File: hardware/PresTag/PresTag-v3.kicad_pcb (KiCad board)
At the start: 2 copper layers, 17 x 9 mm, 20 parts, among them J201 CONN_02X04, J301 Conn_01x01, J302 Conn_01x01, J303 Conn_01x01, J304 Conn_01x01, J401 CONN_01X02, Q501 Q_NPN_BEC, U1 at25ex321D-UUN, U2 LPS27HHWTR, U302 stm32l431kc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

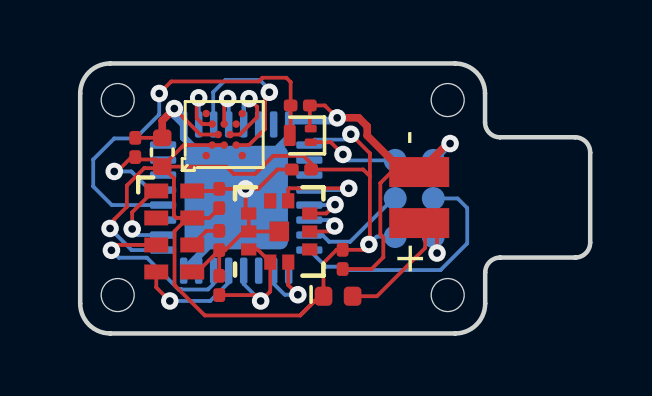
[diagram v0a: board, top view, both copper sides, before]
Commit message: move prestag pcb origin
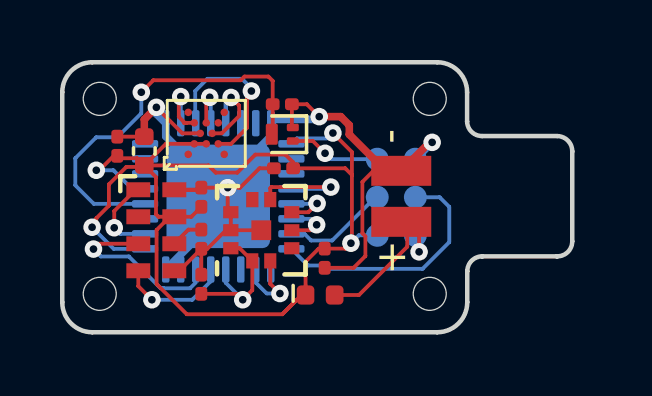
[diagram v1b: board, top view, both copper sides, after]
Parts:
- moved C101 0.60 mm to (146.7, 107.4)
- moved C501 0.60 mm to (148.0, 110.4)
- moved C503 0.60 mm to (143.9, 108.4)
- moved D401 0.60 mm to (147.9, 111.7)
- moved J201 0.60 mm to (150.4, 108.4)
- moved J301 0.60 mm to (150.9, 111.7)
- moved J302 0.60 mm to (150.9, 105.2)
- moved J303 0.60 mm to (139.9, 111.7)
- moved J304 0.60 mm to (139.9, 105.2)
- moved U302 0.60 mm to (144.5, 108.4)
- moved C1 0.60 mm to (143.9, 111.3)
- moved R1 0.60 mm to (143.9, 109.8)
- moved U2 0.60 mm to (145.9, 109.5)
- moved U501 0.60 mm to (142.4, 109.5)
- moved C2 0.60 mm to (141.1, 106.7)
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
